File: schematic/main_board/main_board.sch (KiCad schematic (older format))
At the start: 24 parts, among them J1 To Line OUT, J2 To Line IN, P1 +Vref, P2 GND, P3 -Vref, P4 Probe, P5 GND, U1 LM324N

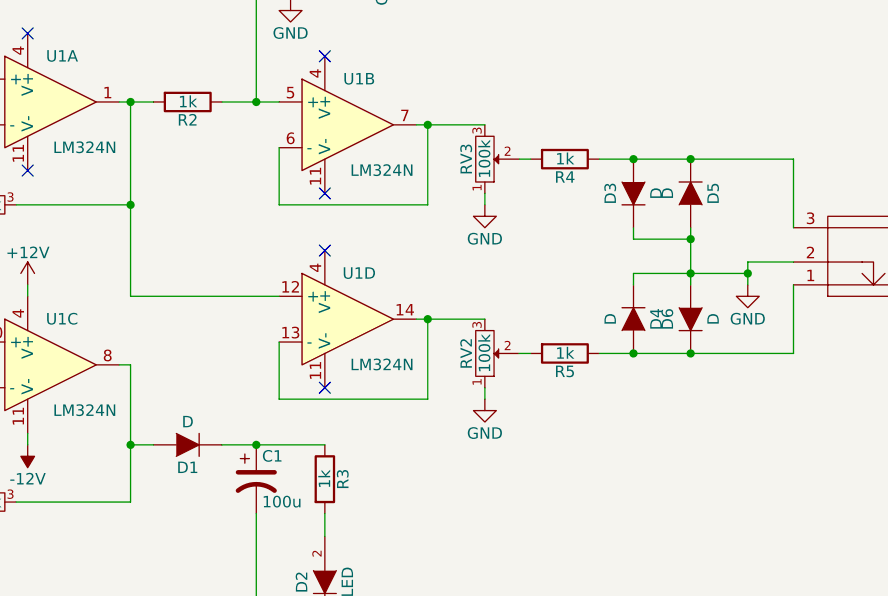
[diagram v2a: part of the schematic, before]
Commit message: Added footprints for some soviet elements which used on Main board.
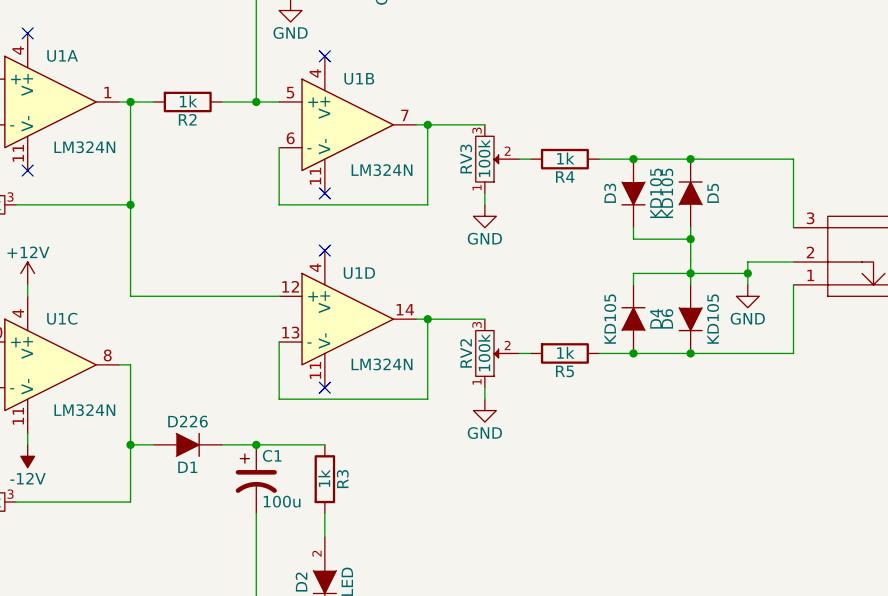
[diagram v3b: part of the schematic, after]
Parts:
- C1: footprint (none) -> footprints:C100u_vert
- D1: value D -> D226; footprint (none) -> footprints:Diode_D226
- D2: footprint (none) -> footprints:Pin_vert_1x02
- D3, D4, D5, D6: value D -> KD105; footprint (none) -> footprints:Diode_KD105
- P1, P2, P3, P4, P5: footprint footprints:1pin_big -> footprints:1pin_small
- R4, R5: footprint (none) -> footprints:Resistor_Horizontal_RM15mm
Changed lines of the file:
@@
 $EndComp
 $Comp
-L GND #PWR7
+L GND #PWR01
 U 1 1 57BD55DE
 P 3200 4400
-F 0 "#PWR7" H 3200 4150 50  0001 C CNN
+F 0 "#PWR01" H 3200 4150 50  0001 C CNN
 F 1 "GND" H 3200 4250 50  0000 C CNN
 F 2 "" H 3200 4400 50  0000 C CNN
@@
 $EndComp
 $Comp
-L GND #PWR12
+L GND #PWR02
 U 1 1 57BD5FBC
 P 5600 3000
-F 0 "#PWR12" H 5600 2750 50  0001 C CNN
+F 0 "#PWR02" H 5600 2750 50  0001 C CNN
 F 1 "GND" H 5600 2850 50  0000 C CNN
 F 2 "" H 5600 3000 50  0000 C CNN
@@
 $EndComp
 $Comp
-L GND #PWR13
+L GND #PWR03
 U 1 1 57BD6135
 P 5600 3850
-F 0 "#PWR13" H 5600 3600 50  0001 C CNN
+F 0 "#PWR03" H 5600 3600 50  0001 C CNN
 F 1 "GND" H 5600 3700 50  0000 C CNN
 F 2 "" H 5600 3850 50  0000 C CNN
@@
 $EndComp
 $Comp
-L GND #PWR6
+L GND #PWR04
 U 1 1 57BD62A5
 P 3200 3100
-F 0 "#PWR6" H 3200 2850 50  0001 C CNN
+F 0 "#PWR04" H 3200 2850 50  0001 C CNN
 F 1 "GND" H 3200 2950 50  0000 C CNN
 F 2 "" H 3200 3100 50  0000 C CNN
@@
 $EndComp
 $Comp
-L GND #PWR5
+L GND #PWR05
 U 1 1 57BD632F
 P 3100 2800
-F 0 "#PWR5" H 3100 2550 50  0001 C CNN
+F 0 "#PWR05" H 3100 2550 50  0001 C CNN
 F 1 "GND" H 3100 2650 50  0000 C CNN
 F 2 "" H 3100 2800 50  0000 C CNN
@@
 NoConn ~ 4900 3800
 $Comp
-L +12V #PWR8
+L +12V #PWR06
 U 1 1 57BD6625
 P 3600 3350
-F 0 "#PWR8" H 3600 3200 50  0001 C CNN
+F 0 "#PWR06" H 3600 3200 50  0001 C CNN
 F 1 "+12V" H 3600 3490 50  0000 C CNN
 F 2 "" H 3600 3350 50  0000 C CNN
@@
 $EndComp
 $Comp
-L PWR_FLAG #FLG1
+L PWR_FLAG #FLG07
 U 1 1 57BD744C
 P 2250 3400
-F 0 "#FLG1" H 2250 3495 50  0001 C CNN
+F 0 "#FLG07" H 2250 3495 50  0001 C CNN
 F 1 "PWR_FLAG" H 2250 3580 50  0000 C CNN
 F 2 "" H 2250 3400 50  0000 C CNN
@@
 F 0 "P1" H 1950 3500 50  0000 C CNN
 F 1 "+Vref" V 2050 3400 50  0000 C CNN
-F 2 "footprints:1pin_big" H 1950 3400 50  0001 C CNN
+F 2 "footprints:1pin_small" H 1950 3400 50  0001 C CNN
 F 3 "" H 1950 3400 50  0000 C CNN
 	1    1950 3400
@@
 $EndComp
 $Comp
-L +12V #PWR1
+L +12V #PWR08
 U 1 1 57BD755B
 P 2600 3400
-F 0 "#PWR1" H 2600 3250 50  0001 C CNN
+F 0 "#PWR08" H 2600 3250 50  0001 C CNN
 F 1 "+12V" H 2600 3540 50  0000 C CNN
 F 2 "" H 2600 3400 50  0000 C CNN
@@
 $EndComp
 $Comp
-L GND #PWR2
+L GND #PWR09
 U 1 1 57BD8243
 P 2600 3800
-F 0 "#PWR2" H 2600 3550 50  0001 C CNN
+F 0 "#PWR09" H 2600 3550 50  0001 C CNN
 F 1 "GND" H 2600 3650 50  0000 C CNN
 F 2 "" H 2600 3800 50  0000 C CNN
@@
 F 0 "P2" H 1950 3900 50  0000 C CNN
 F 1 "GND" V 2050 3800 50  0000 C CNN
-F 2 "footprints:1pin_big" H 1950 3800 50  0001 C CNN
+F 2 "footprints:1pin_small" H 1950 3800 50  0001 C CNN
 F 3 "" H 1950 3800 50  0000 C CNN
 	1    1950 3800
@@
 F 0 "P3" H 1950 4300 50  0000 C CNN
 F 1 "-Vref" V 2050 4200 50  0000 C CNN
-F 2 "footprints:1pin_big" H 1950 4200 50  0001 C CNN
+F 2 "footprints:1pin_small" H 1950 4200 50  0001 C CNN
 F 3 "" H 1950 4200 50  0000 C CNN
 	1    1950 4200
@@
 $EndComp
 $Comp
-L PWR_FLAG #FLG2
+L PWR_FLAG #FLG010
 U 1 1 57BD83E4
 P 2250 3800
-F 0 "#FLG2" H 2250 3895 50  0001 C CNN
+F 0 "#FLG010" H 2250 3895 50  0001 C CNN
 F 1 "PWR_FLAG" H 2250 3980 50  0000 C CNN
 F 2 "" H 2250 3800 50  0000 C CNN
@@
 $EndComp
 $Comp
-L PWR_FLAG #FLG3
+L PWR_FLAG #FLG011
 U 1 1 57BD841C
 P 2250 4200
-F 0 "#FLG3" H 2250 4295 50  0001 C CNN
+F 0 "#FLG011" H 2250 4295 50  0001 C CNN
 F 1 "PWR_FLAG" H 2250 4380 50  0000 C CNN
 F 2 "" H 2250 4200 50  0000 C CNN
@@
 F 0 "P4" H 5050 1900 50  0000 C CNN
 F 1 "Probe" V 5150 1800 50  0000 C CNN
-F 2 "footprints:1pin_big" H 5050 1800 50  0001 C CNN
+F 2 "footprints:1pin_small" H 5050 1800 50  0001 C CNN
 F 3 "" H 5050 1800 50  0000 C CNN
 	1    5050 1800
@@
 F 0 "P5" H 5050 2150 50  0000 C CNN
 F 1 "GND" V 5150 2050 50  0000 C CNN
-F 2 "footprints:1pin_big" H 5050 2050 50  0001 C CNN
+F 2 "footprints:1pin_small" H 5050 2050 50  0001 C CNN
 F 3 "" H 5050 2050 50  0000 C CNN
 	1    5050 2050
@@
 $EndComp
 $Comp
-L GND #PWR11
+L GND #PWR012
 U 1 1 57BD887B
 P 4750 2100
-F 0 "#PWR11" H 4750 1850 50  0001 C CNN
+F 0 "#PWR012" H 4750 1850 50  0001 C CNN
 F 1 "GND" H 4750 1950 50  0000 C CNN
 F 2 "" H 4750 2100 50  0000 C CNN
@@
 NoConn ~ 2550 2700
 $Comp
-L GND #PWR4
+L GND #PWR013
 U 1 1 57BD9647
 P 2750 2800
-F 0 "#PWR4" H 2750 2550 50  0001 C CNN
+F 0 "#PWR013" H 2750 2550 50  0001 C CNN
 F 1 "GND" H 2750 2650 50  0000 C CNN
 F 2 "" H 2750 2800 50  0000 C CNN
@@
 $EndComp
 $Comp
-L GND #PWR14
+L GND #PWR014
 U 1 1 57BD96EB
 P 6750 3350
-F 0 "#PWR14" H 6750 3100 50  0001 C CNN
+F 0 "#PWR014" H 6750 3100 50  0001 C CNN
 F 1 "GND" H 6750 3200 50  0000 C CNN
 F 2 "" H 6750 3350 50  0000 C CNN
@@
 P 4300 4050
 F 0 "D1" H 4300 4150 50  0000 C CNN
-F 1 "D" H 4300 3950 50  0000 C CNN
-F 2 "" H 4300 4050 50  0001 C CNN
+F 1 "D226" H 4300 3950 50  0000 C CNN
+F 2 "footprints:Diode_D226" H 4300 4050 50  0001 C CNN
 F 3 "" H 4300 4050 50  0000 C CNN
 	1    4300 4050
@@
 F 0 "C1" H 4625 4300 50  0000 L CNN
 F 1 "100u" H 4625 4100 50  0000 L CNN
-F 2 "" H 4600 4200 50  0001 C CNN
+F 2 "footprints:C100u_vert" H 4600 4200 50  0001 C CNN
 F 3 "" H 4600 4200 50  0000 C CNN
 	1    4600 4200
@@
 F 0 "D2" H 4900 4750 50  0000 C CNN
 F 1 "LED" H 4900 4550 50  0000 C CNN
-F 2 "" H 4900 4650 50  0001 C CNN
+F 2 "footprints:Pin_vert_1x02" H 4900 4650 50  0001 C CNN
 F 3 "" H 4900 4650 50  0000 C CNN
 	1    4900 4650
@@
 $EndComp
 $Comp
-L GND #PWR10
+L GND #PWR015
 U 1 1 57C3EFA0
 P 4600 4900
-F 0 "#PWR10" H 4600 4650 50  0001 C CNN
+F 0 "#PWR015" H 4600 4650 50  0001 C CNN
 F 1 "GND" H 4600 4750 50  0000 C CNN
 F 2 "" H 4600 4900 50  0000 C CNN
@@
 F 0 "R4" V 6030 2800 50  0000 C CNN
 F 1 "1k" V 5950 2800 50  0000 C CNN
-F 2 "" V 5880 2800 50  0000 C CNN
+F 2 "footprints:Resistor_Horizontal_RM15mm" V 5880 2800 50  0001 C CNN
 F 3 "" H 5950 2800 50  0000 C CNN
 	1    5950 2800
@@
 F 0 "R5" V 6030 3650 50  0000 C CNN
 F 1 "1k" V 5950 3650 50  0000 C CNN
-F 2 "" V 5880 3650 50  0000 C CNN
+F 2 "footprints:Resistor_Horizontal_RM15mm" V 5880 3650 50  0001 C CNN
 F 3 "" H 5950 3650 50  0000 C CNN
 	1    5950 3650
@@
 P 6500 2950
 F 0 "D5" H 6500 3050 50  0000 C CNN
-F 1 "D" H 6500 2850 50  0000 C CNN
-F 2 "" H 6500 2950 50  0000 C CNN
+F 1 "KD105" H 6500 2850 50  0000 C CNN
+F 2 "footprints:Diode_KD105" H 6500 2950 50  0001 C CNN
 F 3 "" H 6500 2950 50  0000 C CNN
 	1    6500 2950
@@
 P 6250 3500
 F 0 "D4" H 6250 3600 50  0000 C CNN
-F 1 "D" H 6250 3400 50  0000 C CNN
-F 2 "" H 6250 3500 50  0000 C CNN
+F 1 "KD105" H 6250 3400 50  0000 C CNN
+F 2 "footprints:Diode_KD105" H 6250 3500 50  0001 C CNN
 F 3 "" H 6250 3500 50  0000 C CNN
 	1    6250 3500
@@
 P 6250 2950
 F 0 "D3" H 6250 3050 50  0000 C CNN
-F 1 "D" H 6250 2850 50  0000 C CNN
-F 2 "" H 6250 2950 50  0000 C CNN
+F 1 "KD105" H 6250 2850 50  0000 C CNN
+F 2 "footprints:Diode_KD105" H 6250 2950 50  0001 C CNN
 F 3 "" H 6250 2950 50  0000 C CNN
 	1    6250 2950
@@
 P 6500 3500
 F 0 "D6" H 6500 3600 50  0000 C CNN
-F 1 "D" H 6500 3400 50  0000 C CNN
-F 2 "" H 6500 3500 50  0000 C CNN
+F 1 "KD105" H 6500 3400 50  0000 C CNN
+F 2 "footprints:Diode_KD105" H 6500 3500 50  0001 C CNN
 F 3 "" H 6500 3500 50  0000 C CNN
 	1    6500 3500

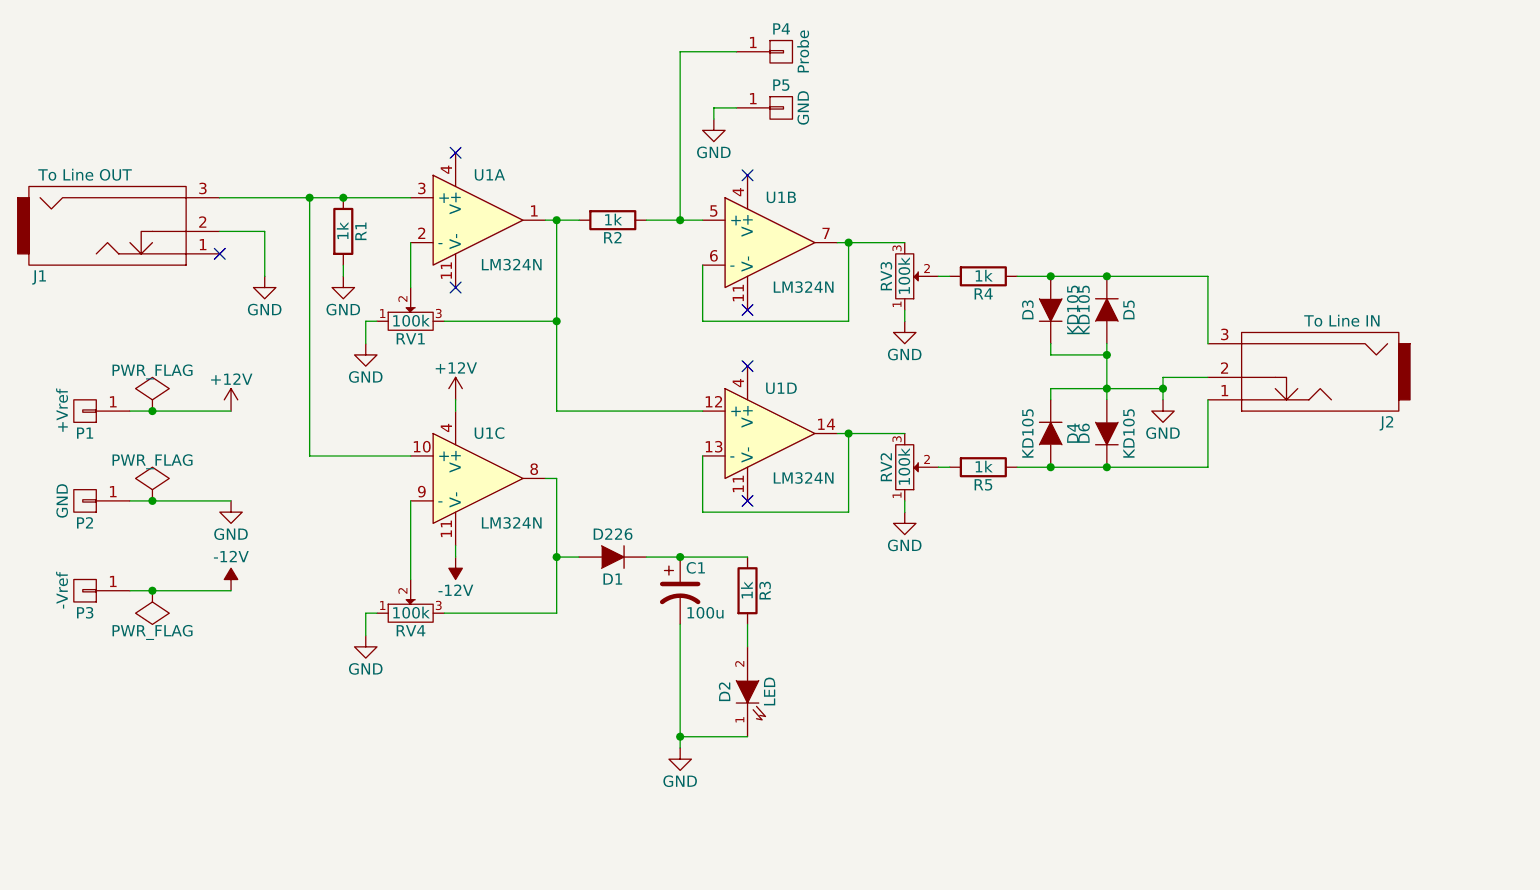
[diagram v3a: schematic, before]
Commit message: Added 0.1u capacitors and filled zones to PCB.
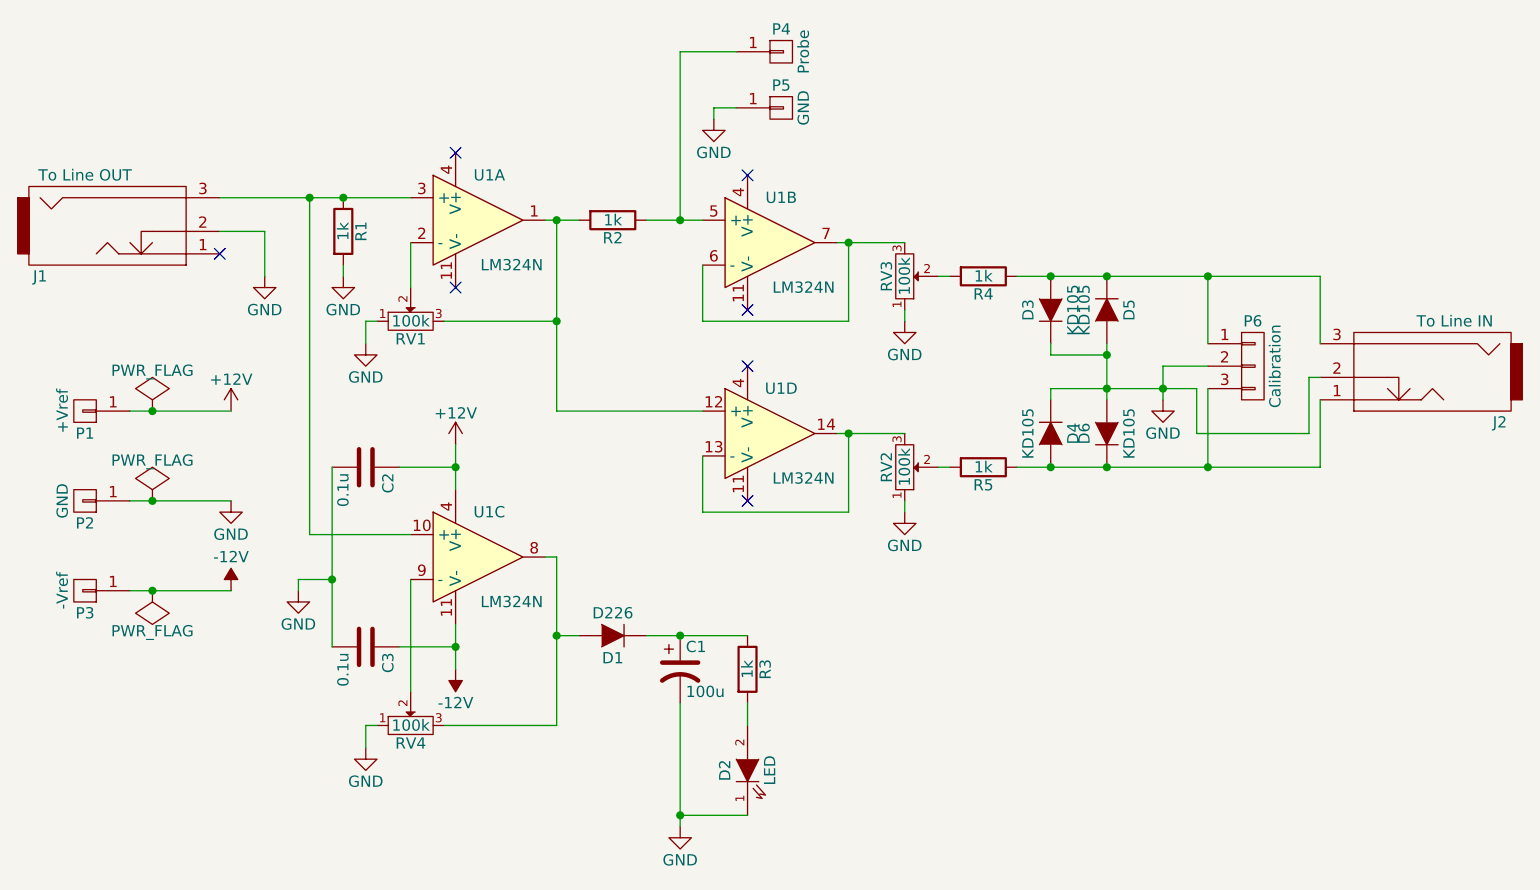
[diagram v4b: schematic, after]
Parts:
- added C2, C3: 0.1u, footprints:C_0.1u, symbol C
- added P6: Calibration, Connect:PINHEAD1-3, symbol CONN_01X03
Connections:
- net +12V: now also C2.1
- net -12V: now also C3.1
- net GND: now also C2.2, C3.2, P6.2 (P2)
- net at D4.2 (A), D6.1 (K), J2.1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: now also P6.3 (P3)
- net at D3.2 (A), D5.1 (K), J2.3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: now also P6.1 (P1)
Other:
- moved on the sheet: C1, D1, D2, J2, R3, RV4, U1C
